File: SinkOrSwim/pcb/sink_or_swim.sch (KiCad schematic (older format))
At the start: 3 parts, among them P101 CONN_01X02, P102 CONN_01X03, P103 CONN_01X02

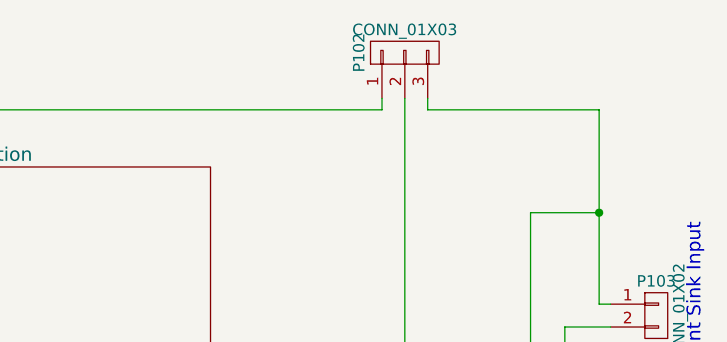
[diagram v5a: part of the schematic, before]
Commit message: Switched pin headers for terminal blocks for batt and self-powered from sink.  PCB is WIP.
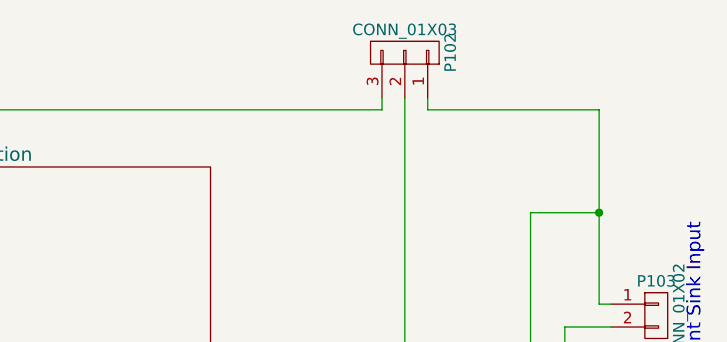
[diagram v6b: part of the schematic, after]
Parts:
- P101, P103: footprint Pin_Headers:Pin_Header_Straight_1x02 -> pcb:OSTTA024163
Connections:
- net CurrentControl/Current_Sink+: now also P102.1 (P1); no longer P102.3 (P3)
- net at P101.1 (P1): now also P102.3 (P3); no longer P102.1 (P1)
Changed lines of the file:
@@
 Comment4 ""
 $EndDescr
-Wire Wire Line
-	8550 2100 8550 6150
-Wire Wire Line
-	8550 2100 8750 2100
 $Comp
 L CONN_01X03 P102
@@
 F 3 "" H 7850 900 60  0000 C CNN
 	1    7850 900
-	0    -1   -1   0
+	0    1    -1   0
 $EndComp
-Wire Wire Line
-	7850 1100 7850 2300
 $Comp
 L CONN_01X02 P101
@@
 F 0 "P101" H 4450 1350 50  0000 C CNN
 F 1 "CONN_01X02" V 4550 1200 50  0000 C CNN
-F 2 "Pin_Headers:Pin_Header_Straight_1x02" H 4450 1200 60  0001 C CNN
+F 2 "pcb:OSTTA024163" H 4450 1200 60  0001 C CNN
 F 3 "" H 4450 1200 60  0000 C CNN
 	1    4450 1200
 	-1   0    0    -1
 $EndComp
-Wire Wire Line
-	4650 1150 7750 1150
 $Comp
 L GND #PWR01
@@
 F2 "Vin" I R 7000 2300 60
 $EndSheet
+$Comp
+L GND #PWR02
+U 1 1 54DC7B33
+P 8550 6150
+F 0 "#PWR02" H 8550 5900 60  0001 C CNN
+F 1 "GND" H 8550 6000 60  0000 C CNN
+F 2 "" H 8550 6150 60  0000 C CNN
+F 3 "" H 8550 6150 60  0000 C CNN
+	1    8550 6150
+	1    0    0    -1
+$EndComp
+$Comp
+L CONN_01X02 P103
+U 1 1 54D1894C
+P 8950 2050
+F 0 "P103" H 8950 2200 50  0000 C CNN
+F 1 "CONN_01X02" V 9050 2050 50  0000 C CNN
+F 2 "pcb:OSTTA024163" H 8950 2050 60  0001 C CNN
+F 3 "" H 8950 2050 60  0000 C CNN
+	1    8950 2050
+	1    0    0    -1
+$EndComp
+Wire Wire Line
+	8550 2100 8550 6150
+Wire Wire Line
+	8550 2100 8750 2100
+Wire Wire Line
+	7850 1100 7850 2300
+Wire Wire Line
+	4650 1150 7750 1150
 Wire Wire Line
 	8700 1600 8400 1600
@@
 	5200 4800 5400 4800
 Connection ~ 8550 5950
-$Comp
-L GND #PWR02
-U 1 1 54DC7B33
-P 8550 6150
-F 0 "#PWR02" H 8550 5900 60  0001 C CNN
-F 1 "GND" H 8550 6000 60  0000 C CNN
-F 2 "" H 8550 6150 60  0000 C CNN
-F 3 "" H 8550 6150 60  0000 C CNN
-	1    8550 6150
-	1    0    0    -1
-$EndComp
 Wire Wire Line
 	4650 1250 4750 1250
@@
 Wire Wire Line
 	7950 1150 8700 1150
-$Comp
-L CONN_01X02 P103
-U 1 1 54D1894C
-P 8950 2050
-F 0 "P103" H 8950 2200 50  0000 C CNN
-F 1 "CONN_01X02" V 9050 2050 50  0000 C CNN
-F 2 "Pin_Headers:Pin_Header_Straight_1x02" H 8950 2050 60  0001 C CNN
-F 3 "" H 8950 2050 60  0000 C CNN
-	1    8950 2050
-	1    0    0    -1
-$EndComp
 Wire Wire Line
 	8700 1150 8700 2000

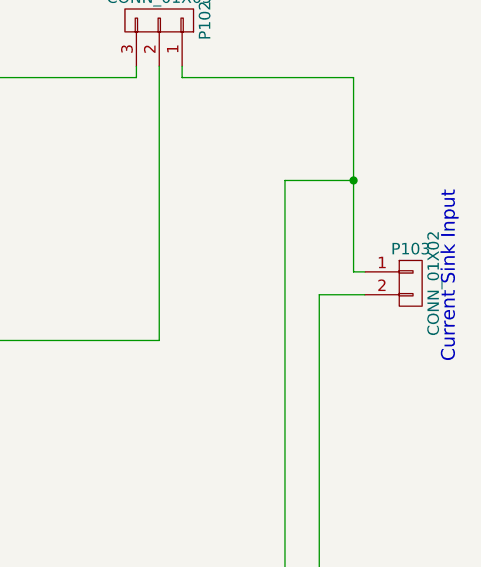
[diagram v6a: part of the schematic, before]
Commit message: More pcb layout changes.  Looks better now.
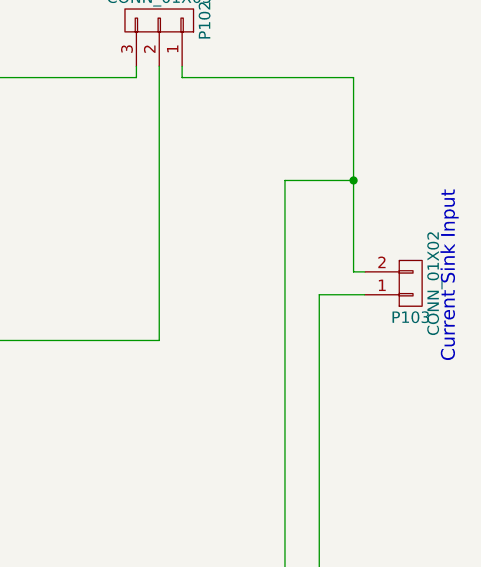
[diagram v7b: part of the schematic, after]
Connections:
- net CurrentControl/Current_Sink+: now also P103.2 (P2); no longer P103.1 (P1)
- net GND: now also P103.1 (P1); no longer P103.2 (P2)
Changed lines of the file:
@@
 F 3 "" H 8950 2050 60  0000 C CNN
 	1    8950 2050
-	1    0    0    -1
+	1    0    0    1
 $EndComp
 Wire Wire Line

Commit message: Gerbers added, BOM written
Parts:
- P101, P103: value CONN_01X02 -> TERMINAL_BLOCK; MPN (none) -> OSTTA024163
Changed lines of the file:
@@
 P 4450 1200
 F 0 "P101" H 4450 1350 50  0000 C CNN
-F 1 "CONN_01X02" V 4550 1200 50  0000 C CNN
+F 1 "TERMINAL_BLOCK" V 4550 1200 50  0000 C CNN
 F 2 "pcb:OSTTA024163" H 4450 1200 60  0001 C CNN
-F 3 "" H 4450 1200 60  0000 C CNN
+F 3 "http://www.on-shore.com/sites/default/files/manuals/OSTTAXX4163.pdf" H 4450 1200 60  0001 C CNN
+F 4 "OSTTA024163" H 4450 1200 60  0001 C CNN "MPN"
 	1    4450 1200
 	-1   0    0    -1
@@
 P 8950 2050
 F 0 "P103" H 8950 2200 50  0000 C CNN
-F 1 "CONN_01X02" V 9050 2050 50  0000 C CNN
+F 1 "TERMINAL_BLOCK" V 9050 2050 50  0000 C CNN
 F 2 "pcb:OSTTA024163" H 8950 2050 60  0001 C CNN
-F 3 "" H 8950 2050 60  0000 C CNN
+F 3 "http://www.on-shore.com/sites/default/files/manuals/OSTTAXX4163.pdf" H 8950 2050 60  0001 C CNN
+F 4 "OSTTA024163" H 8950 2050 60  0001 C CNN "MPN"
 	1    8950 2050
 	1    0    0    1
